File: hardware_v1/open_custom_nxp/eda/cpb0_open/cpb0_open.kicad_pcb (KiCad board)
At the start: 2 copper layers, 200 x 150 mm, 0 parts

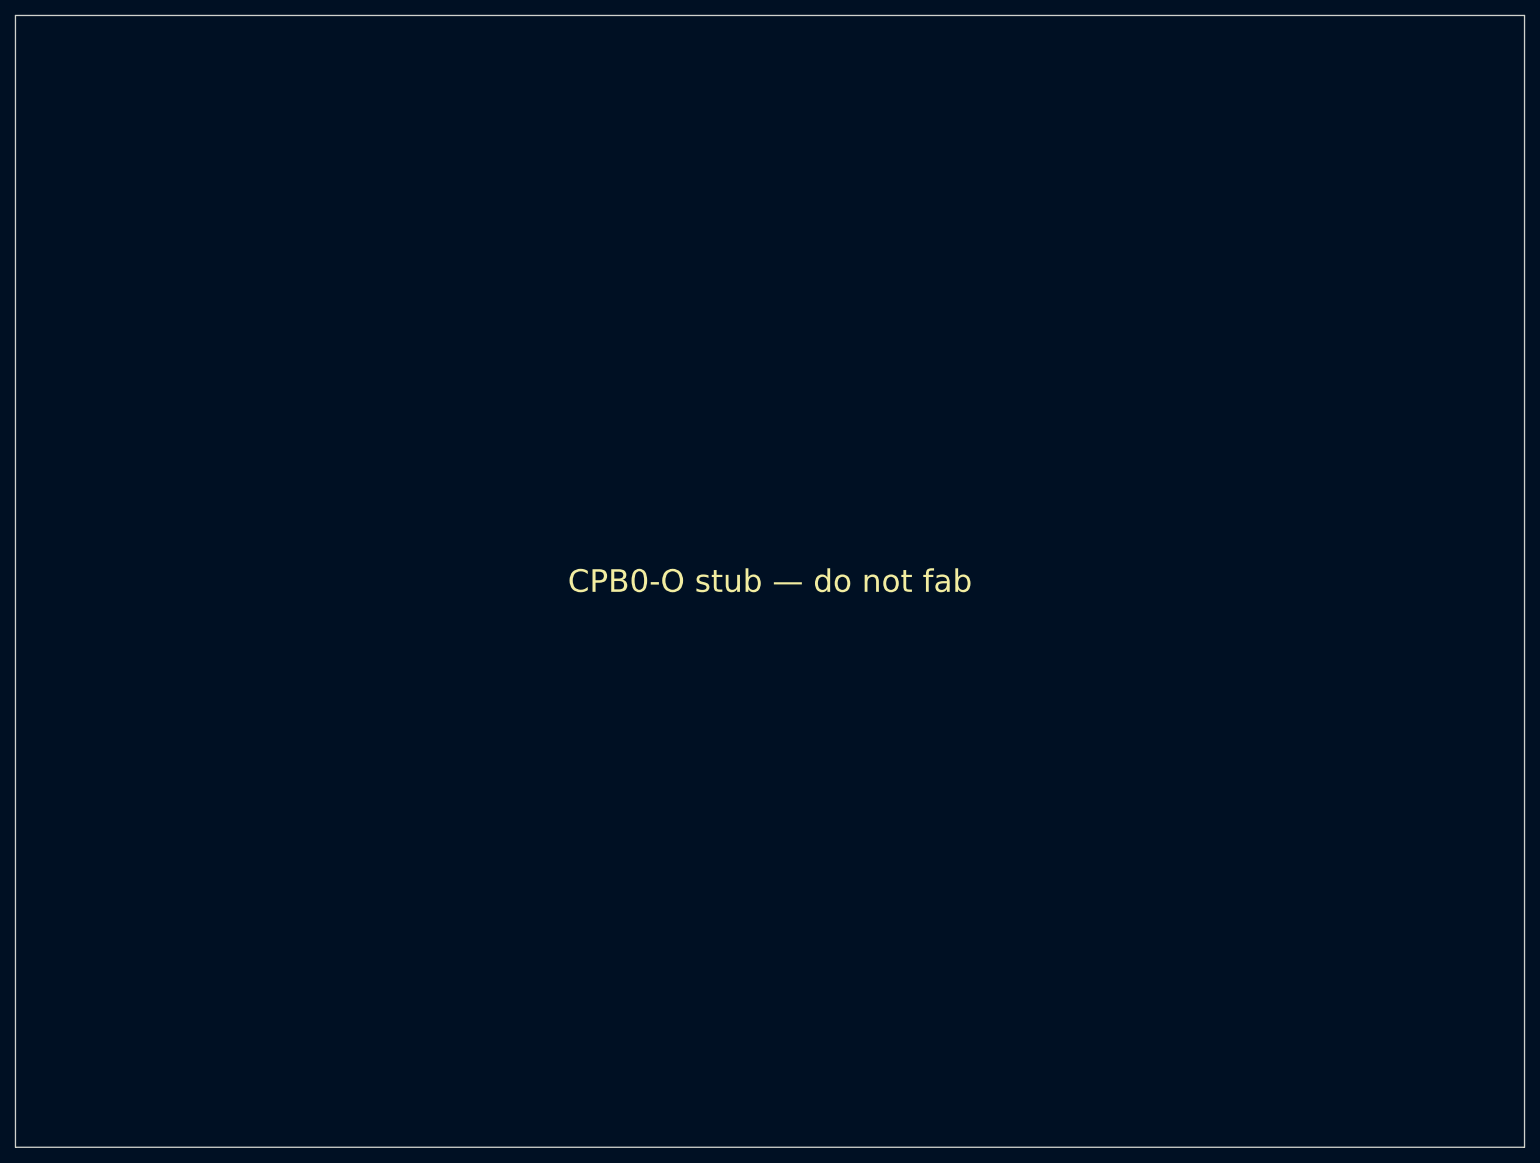
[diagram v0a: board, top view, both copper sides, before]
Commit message: feat(nxp): implement CPB0 placement routing and constraints
Define a 14-layer design stackup, board outline/placement zones, and SI/PI matrices without claiming DRC or SI/PI pass.

Co-authored-by: Cursor <cursoragent@cursor.com>
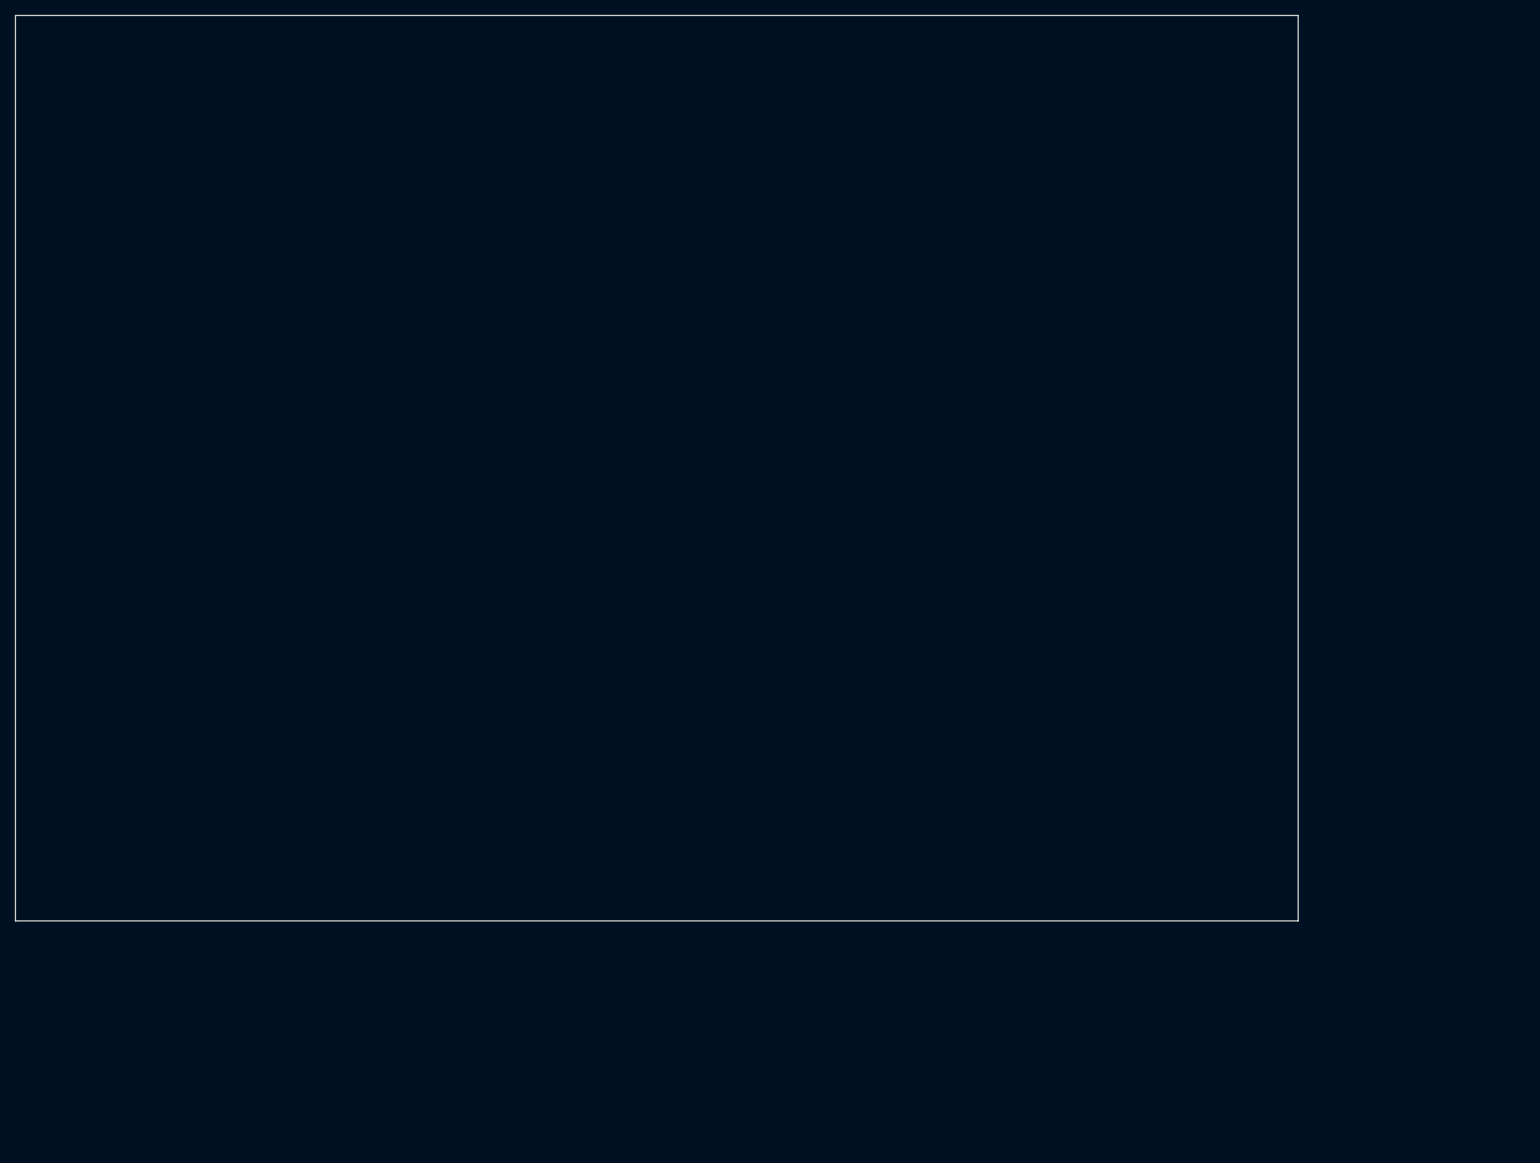
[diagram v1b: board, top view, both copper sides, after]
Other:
- board size 200 x 150 mm -> 170 x 120 mm
- copper layers 2 -> 5
- rule pad_to_mask_clearance: 0 -> 0.05
- board text added: "CPB0-O placement stub — not DRC complete; DDR routing blocked on UG10210"
- board text added: "ZONE: M.2"
- board text added: "ZONE: PF09/PF53"
- board text added: "ZONE: SoC+LPDDR"
- board text added: "ZONE: USB/ETH/DEBUG"
- board text removed: "CPB0-O stub — do not fab"
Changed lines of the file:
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@@
-(kicad_pcb (version 20241229) (generator "nxp0_campaign") (generator_version "10.0")
+(kicad_pcb
+  (version 20221018)
+  (generator "nxp1_cpb0_open")
   (general (thickness 1.6) (legacy_teardrops no))
   (paper "A3")
-  (title_block
-    (title "CPB0-O PCB stub")
-    (date "2026-09-18")
-    (rev "0.0.1-nxp0")
-    (company "gunnchOS3k / NXP-0")
-    (comment 1 "NON-ROUTED STUB — layout not started for gate purposes")
-    (comment 2 "CPB0_OPEN_PCB_STARTED=false")
-  )
   (layers
     (0 "F.Cu" signal)
-    (31 "B.Cu" signal)
-    (32 "B.Adhes" user "B.Adhesive")
-    (33 "F.Adhes" user "F.Adhesive")
-    (34 "B.Paste" user)
-    (35 "F.Paste" user)
-    (36 "B.SilkS" user "B.Silkscreen")
-    (37 "F.SilkS" user "F.Silkscreen")
-    (38 "B.Mask" user)
-    (39 "F.Mask" user)
-    (44 "Edge.Cuts" user)
-    (46 "B.CrtYd" user "B.Courtyard")
-    (47 "F.CrtYd" user "F.Courtyard")
+    (1 "In1.Cu" signal)
+    (2 "In2.Cu" power)
+    (3 "In3.Cu" power)
+    (4 "B.Cu" signal)
+    (9 "F.Adhes" user)
+    (11 "B.Adhes" user)
+    (13 "F.Paste" user)
+    (15 "B.Paste" user)
+    (17 "F.SilkS" user)
+    (19 "B.SilkS" user)
+    (21 "F.Mask" user)
+    (23 "B.Mask" user)
+    (25 "Dwgs.User" user)
+    (27 "Cmts.User" user)
+    (29 "Eco1.User" user)
+    (31 "Eco2.User" user)
+    (33 "Edge.Cuts" user)
+    (35 "F.CrtYd" user)
+    (37 "B.CrtYd" user)
+    (39 "F.Fab" user)
+    (41 "B.Fab" user)
   )
-  (setup (pad_to_mask_clearance 0) (allow_soldermask_bridges_in_footprints no))
-  (gr_rect (start 0 0) (end 200 150)
-    (stroke (width 0.1) (type default)) (fill none) (layer "Edge.Cuts"))
-  (gr_text "CPB0-O stub — do not fab" (at 100 75 0) (layer "F.SilkS")
-    (effects (font (size 3 3))))
-  (embedded_fonts no)
+  (setup
+    (pad_to_mask_clearance 0.05)
+    (allow_soldermask_bridges_in_footprints no)
+    (pcbplotparams (layerselection 0x00010fc_ffffffff) (plot_on_all_layers_selection 0x0000000_00000000)
+      (disableapertmacros no) (usegerberextensions no) (usegerberattributes yes) (usegerberadvancedattributes yes)
+      (creategerberjobfile yes) (dashed_line_dash_ratio 12.000000) (dashed_line_gap_ratio 3.000000)
+      (svgprecision 4) (plotframeref no) (viasonmask no) (mode 1) (useauxorigin no) (hpglpennumber 1)
+      (hpglpenspeed 20) (hpglpendiameter 15.000000) (dxfpolygonmode yes) (dxfimperialunits yes)
+      (dxfusepcbnewfont yes) (psnegative no) (psa4output no) (plotreference yes) (plotvalue yes)
+      (plotinvisibletext no) (sketchpadsonfab no) (subtractmaskfromsilk no) (outputformat 1)
+      (mirror no) (drillshape 1) (scaleselection 1) (outputdirectory ""))
+  )
+  (gr_rect (start 0 0) (end 170 120) (stroke (width 0.1) (type solid)) (fill none) (layer "Edge.Cuts"))
+  (gr_text "CPB0-O placement stub — not DRC complete; DDR routing blocked on UG10210"
+    (at 85 10) (layer "Cmts.User")
+    (effects (font (size 2 2) (thickness 0.3))))
+  (gr_text "ZONE: SoC+LPDDR" (at 50 55) (layer "Cmts.User")
+    (effects (font (size 1.5 1.5) (thickness 0.2))))
+  (gr_text "ZONE: PF09/PF53" (at 20 30) (layer "Cmts.User")
+    (effects (font (size 1.5 1.5) (thickness 0.2))))
+  (gr_text "ZONE: M.2" (at 140 55) (layer "Cmts.User")
+    (effects (font (size 1.5 1.5) (thickness 0.2))))
+  (gr_text "ZONE: USB/ETH/DEBUG" (at 85 105) (layer "Cmts.User")
+    (effects (font (size 1.5 1.5) (thickness 0.2))))
 )
